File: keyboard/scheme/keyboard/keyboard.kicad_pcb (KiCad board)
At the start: 2 copper layers, 53 parts

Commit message: Update keyboard pcd
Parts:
- removed the REF** at (62.9, 64.1)
- removed the REF** at (29.8, 88.9)
- removed the REF** at (79.4, 97.2)
- removed the REF** at (29.8, 64.1)
- removed the REF** at (104.1, 64.1)
- removed the REF** at (95.9, 64.1)
- removed the REF** at (112.4, 80.6)
- removed the REF** at (46.4, 97.2)
- removed the REF** at (71.1, 64.1)
- removed the REF** at (38.1, 64.1)
- removed the REF** at (38.1, 88.9)
- removed the REF** at (38.1, 97.2)
- removed the REF** at (112.4, 72.4)
- removed the REF** at (34.3, 80.6)
- removed the REF** at (46.4, 72.4)
- removed the REF** at (79.4, 64.1)
- removed the REF** at (29.8, 97.2)
- removed the REF** at (46.4, 88.9)
- removed the REF** at (46.4, 64.1)
- removed the REF** at (54.6, 64.1)
- removed the REF** at (87.6, 64.1)
- removed the REF** at (112.4, 64.1)
- removed the REF** at (38.1, 72.4)
- removed the REF** at (29.8, 72.4)
- removed the REF** at (42.5, 80.6)
- removed the REF** at (50.8, 80.6)
- added SW1: SW_DIP_x01, my_lib:btn_8x8, F.Cu at (48.9, 88.6)
- added SW10: SW_DIP_x01, my_lib:btn_8x8, F.Cu at (48.9, 105.1)
- added SW11: SW_DIP_x01, my_lib:btn_8x8, F.Cu at (57.1, 105.1)
- added SW12: SW_DIP_x01, my_lib:btn_8x8, F.Cu at (57.1, 113.3)
- added SW13: SW_DIP_x01, my_lib:btn_8x8, F.Cu at (73.7, 88.6)
- added SW14: SW_DIP_x01, my_lib:btn_8x8, F.Cu at (65.4, 88.6)
- added SW15: SW_DIP_x01, my_lib:btn_8x8, F.Cu at (78.1, 96.8)
- added SW16: SW_DIP_x01, my_lib:btn_8x8, F.Cu at (69.8, 96.8)
- added SW17: SW_DIP_x01, my_lib:btn_8x8, F.Cu at (65.4, 105.1)
- added SW18: SW_DIP_x01, my_lib:btn_8x8, F.Cu at (73.7, 105.1)
- added SW19: SW_DIP_x01, my_lib:btn_8x8, F.Cu at (81.9, 88.6)
- added SW2: SW_DIP_x01, my_lib:btn_8x8, F.Cu at (40.6, 88.6)
- added SW20: SW_DIP_x01, my_lib:btn_8x8, F.Cu at (90.2, 88.6)
- added SW21: SW_DIP_x01, my_lib:btn_8x8, F.Cu at (81.9, 105.1)
- added SW22: SW_DIP_x01, my_lib:btn_8x8, F.Cu at (86.4, 96.8)
- added SW23: SW_DIP_x01, my_lib:btn_8x8, F.Cu at (90.2, 105.1)
- added SW24: SW_DIP_x01, my_lib:btn_8x8, F.Cu at (73.7, 113.3)
- added SW25: SW_DIP_x01, my_lib:btn_8x8, F.Cu at (98.4, 88.6)
- added SW26: SW_DIP_x01, my_lib:btn_8x8, F.Cu at (94.6, 96.8)
- added SW27: SW_DIP_x01, my_lib:btn_8x8, F.Cu at (102.9, 96.8)
- added SW28: SW_DIP_x01, my_lib:btn_8x8, F.Cu at (106.7, 105.1)
- added SW29: SW_DIP_x01, my_lib:btn_8x8, F.Cu at (98.4, 105.1)
- added SW3: SW_DIP_x01, my_lib:btn_8x8, F.Cu at (45.1, 96.8)
- added SW30: SW_DIP_x01, my_lib:btn_8x8, F.Cu at (98.4, 113.3)
- added SW31: SW_DIP_x01, my_lib:btn_8x8, F.Cu at (106.7, 88.6)
- added SW32: SW_DIP_x01, my_lib:btn_8x8, F.Cu at (114.9, 88.6)
- added SW33: SW_DIP_x01, my_lib:btn_8x8, F.Cu at (111.1, 96.8)
- added SW34: SW_DIP_x01, my_lib:btn_8x8, F.Cu at (114.9, 105.1)
- added SW35: SW_DIP_x01, my_lib:btn_8x8, F.Cu at (114.9, 113.3)
- added SW36: SW_DIP_x01, my_lib:btn_8x8, F.Cu at (106.7, 113.3)
- added SW4: SW_DIP_x01, my_lib:btn_8x8, F.Cu at (40.6, 105.1)
- added SW5: SW_DIP_x01, my_lib:btn_8x8, F.Cu at (40.6, 113.3)
- added SW6: SW_DIP_x01, my_lib:btn_8x8, F.Cu at (48.9, 113.3)
- added SW7: SW_DIP_x01, my_lib:btn_8x8, F.Cu at (57.1, 88.6)
- added SW8: SW_DIP_x01, my_lib:btn_8x8, F.Cu at (61.6, 96.8)
- added SW9: SW_DIP_x01, my_lib:btn_8x8, F.Cu at (53.3, 96.8)
- added U1: STM32F030F4Px, Package_SO:TSSOP-20_4.4x6.5mm_P0.65mm, F.Cu at (69.8, 119.7)
- moved REF** 38.8 mm to (71.5, 50.1)
- moved REF** 38.8 mm to (104.5, 50.1)
- moved REF** 38.8 mm to (63.2, 50.1)
- moved REF** 38.8 mm to (79.7, 50.1)
- moved REF** 38.8 mm to (55.0, 50.1)
- moved REF** 38.8 mm to (88.0, 50.1)
- moved REF** 38.8 mm to (96.2, 50.1)
- moved REF** 38.8 mm to (88.0, 58.4)
- moved REF** 38.8 mm to (55.0, 33.6)
- moved REF** 38.8 mm to (104.5, 58.4)
- moved REF** 38.8 mm to (63.2, 58.4)
- moved REF** 38.8 mm to (104.5, 33.6)
- moved REF** 38.8 mm to (79.7, 33.6)
- moved REF** 38.8 mm to (63.2, 33.6)
- moved REF** 38.8 mm to (52.1, 56.5)
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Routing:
- net row_2: track 0.00 -> 227.6 mm, vias 0 -> 1
- net row_3: track 0.00 -> 174.9 mm, vias 0 -> 1
- net row_1: track 0.00 -> 158.2 mm, vias 0 -> 1
- net row_4: track 0.00 -> 141.3 mm, vias 0 -> 1
- net row_5: track 0.00 -> 134.0 mm, vias 0 -> 1
- net row_6: track 0.00 -> 94.6 mm, vias 0 -> 1
- net column_6: track 0.00 -> 84.9 mm
- net column_1: track 0.00 -> 83.1 mm
- net column_5: track 0.00 -> 76.0 mm
- net column_2: track 0.00 -> 61.7 mm
- net column_3: track 0.00 -> 61.6 mm
- net column_4: track 0.00 -> 61.2 mm
- net sw_dio: track 0.00 -> 16.2 mm, vias 0 -> 1
- net sw_clk: track 0.00 -> 11.2 mm, vias 0 -> 1

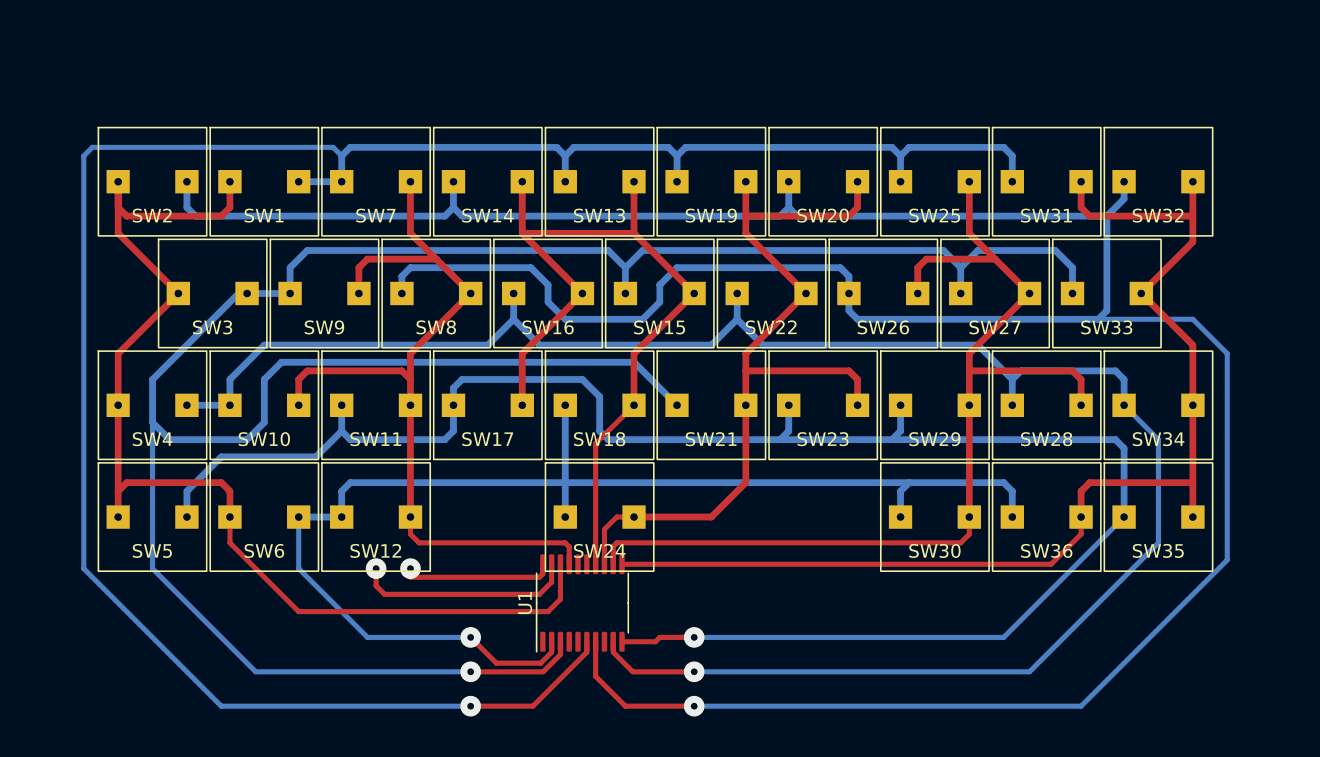
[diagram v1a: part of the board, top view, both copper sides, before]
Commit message: Add power supply to keyboard scheme
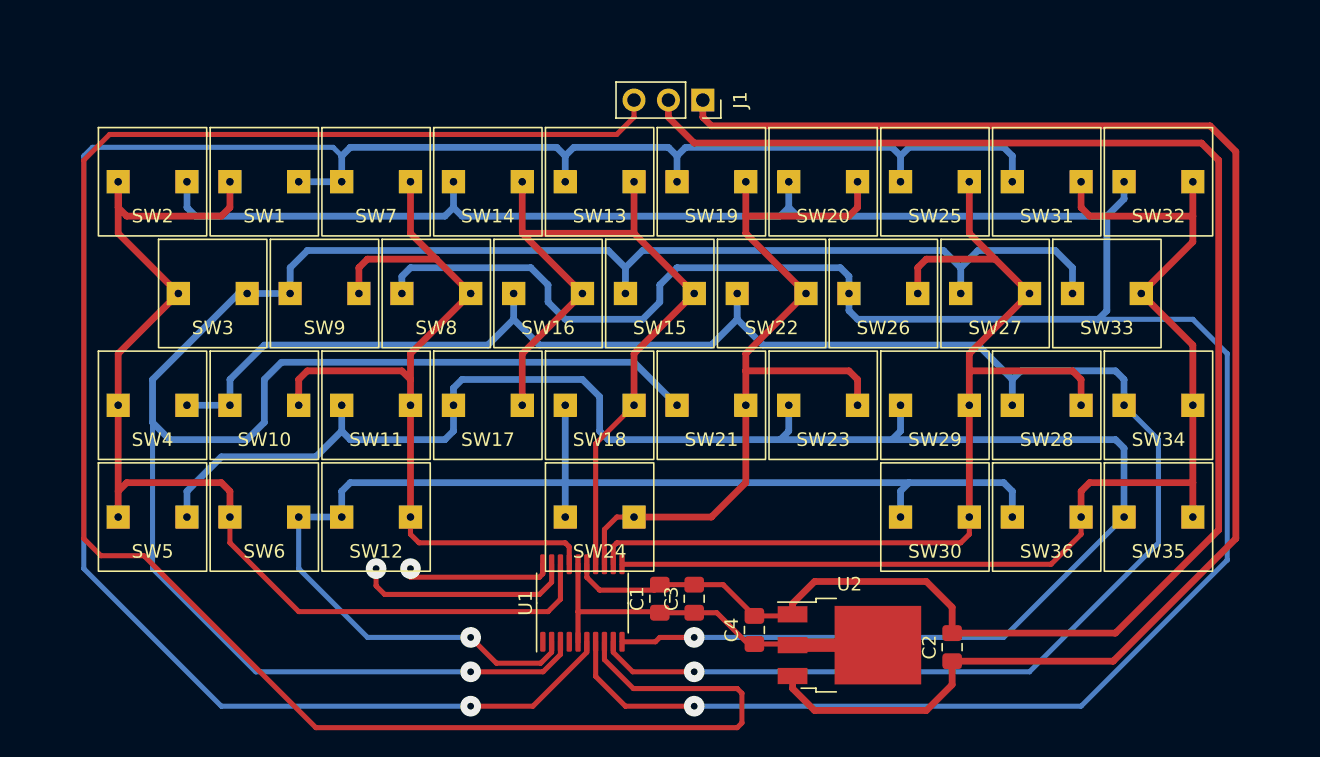
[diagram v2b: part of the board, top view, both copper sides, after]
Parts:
- added C1: 100nF, Capacitor_SMD:C_0805_2012Metric_Pad1.18x1.45mm_HandSolder, F.Cu at (75.6, 119.4)
- added C2: 10mF, Capacitor_SMD:C_0805_2012Metric_Pad1.18x1.45mm_HandSolder, F.Cu at (97.2, 123.0)
- added C3: 4.7mF, Capacitor_SMD:C_0805_2012Metric_Pad1.18x1.45mm_HandSolder, F.Cu at (78.1, 119.4)
- added C4: 22mF, Capacitor_SMD:C_0805_2012Metric_Pad1.18x1.45mm_HandSolder, F.Cu at (82.5, 121.7)
- added J1: Conn_01x03, Connector_PinSocket_2.54mm:PinSocket_1x03_P2.54mm_Vertical, F.Cu at (78.7, 82.5)
- added U2: AMS1117CD-3.3, Package_TO_SOT_SMD:TO-252-3_TabPin2, F.Cu at (89.6, 122.8)
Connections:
- U1 pad 15: unconnected-(U1-Pad15) -> GND
- U1 pad 16: unconnected-(U1-Pad16) -> 3.3v
- U1 pad 5: unconnected-(U1-Pad5) -> 3.3v
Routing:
- net uart_tx: track 0.00 -> 140.4 mm
- net GND: track 0.00 -> 127.0 mm
- net 5v: track 0.00 -> 110.9 mm
- net 3.3v: track 0.00 -> 28.9 mm

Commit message: Some fix keyboard scheme
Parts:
- removed REF**: PinHeader_1x07_P2.54mm_Vertical, Connector_PinHeader_2.54mm:PinHeader_1x07_P2.54mm_Vertical
- removed REF** (x24): btn_8x8, my_footprints:btn_8x8
- removed REF**: PinHeader_1x08_P2.54mm_Vertical, Connector_PinHeader_2.54mm:PinHeader_1x08_P2.54mm_Vertical
- removed REF**: R_1206_3216Metric_Pad1.30x1.75mm_HandSolder, Resistor_SMD:R_1206_3216Metric_Pad1.30x1.75mm_HandSolder
- moved J1 2.13 mm to (77.8, 84.5)
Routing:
- net (no net): track 1683.9 -> 0.00 mm
- net uart_tx: track 140.4 -> 137.9 mm
- net GND: track 127.0 -> 127.8 mm
- net 5v: track 110.9 -> 110.3 mm

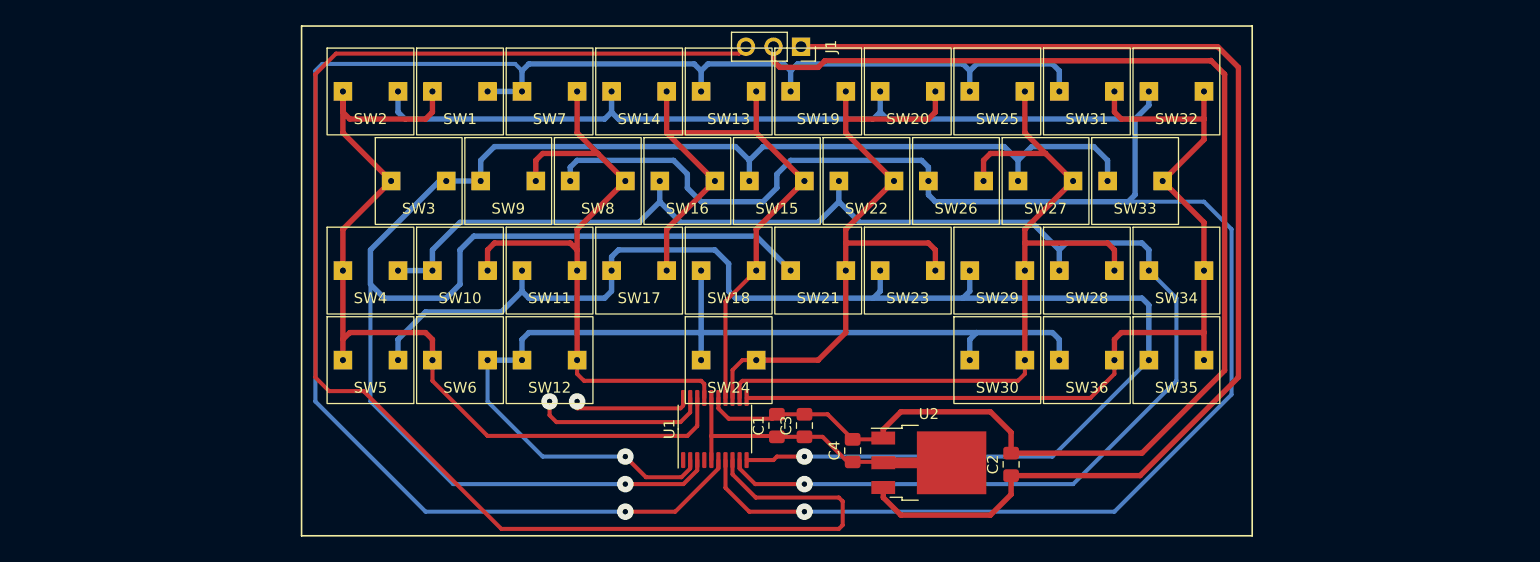
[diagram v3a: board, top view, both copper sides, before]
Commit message: Add copyright to keyboard scheme
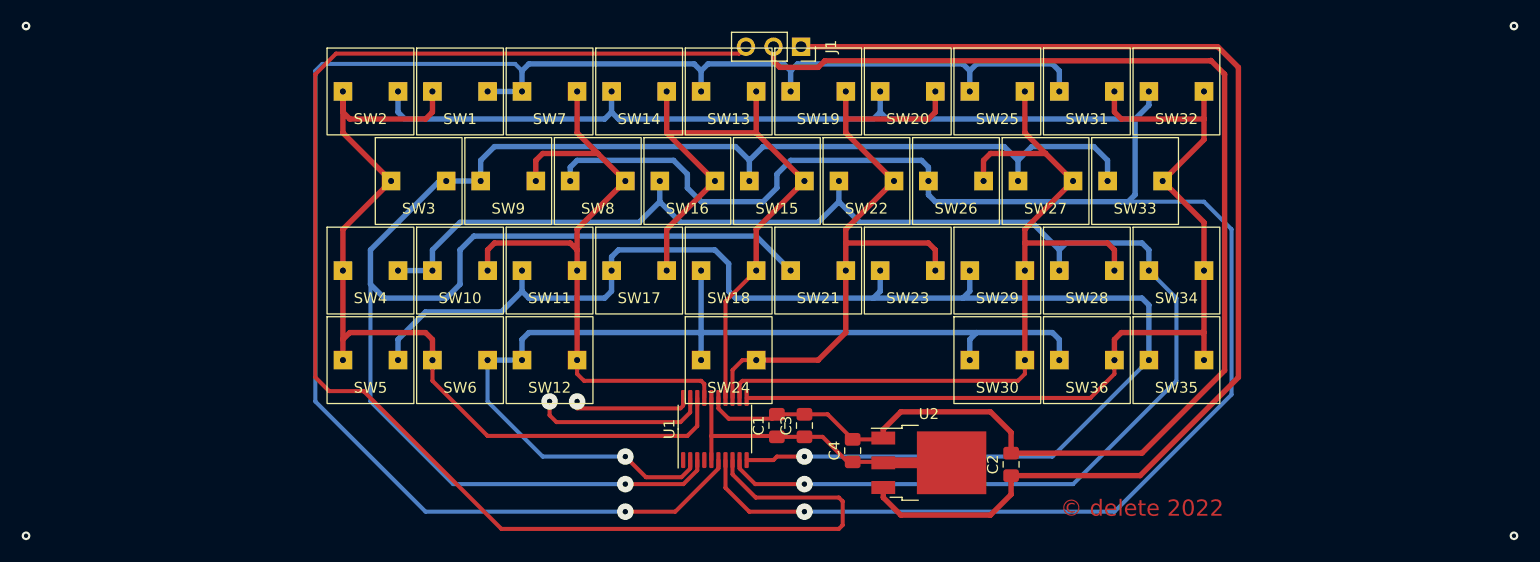
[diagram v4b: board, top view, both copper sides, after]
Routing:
- net (no net): vias 0 -> 4
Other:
- board text added: "© delete 2022"
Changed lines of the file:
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@@
     )
   )
-  (gr_rect (start 119.38 129.54) (end 31.75 82.55) (layer "F.SilkS") (width 0.15) (fill none))
+  (gr_rect (start 119.38 129.54) (end 31.75 82.55) (layer "F.Mask") (width 0.15) (fill none))
+  (gr_text "© delete 2022" (at 109.22 127) (layer "F.Cu")
+    (effects (font (size 1.5 1.5) (thickness 0.3)))
+  )
+  (via (at 143.51 82.55) (size 0.8) (drill 0.4) (layers "F.Cu" "B.Cu") (free) (net 0))
+  (via (at 6.35 129.54) (size 0.8) (drill 0.4) (layers "F.Cu" "B.Cu") (free) (net 0))
+  (via (at 6.35 82.55) (size 0.8) (drill 0.4) (layers "F.Cu" "B.Cu") (free) (net 0))
+  (via (at 143.51 129.54) (size 0.8) (drill 0.4) (layers "F.Cu" "B.Cu") (free) (net 0))
   (segment (start 82.085 122.725) (end 79.7775 120.4175) (width 0.375) (layer "F.Cu") (net 3))
   (segment (start 75.565 120.4175) (end 78.105 120.4175) (width 0.375) (layer "F.Cu") (net 3))

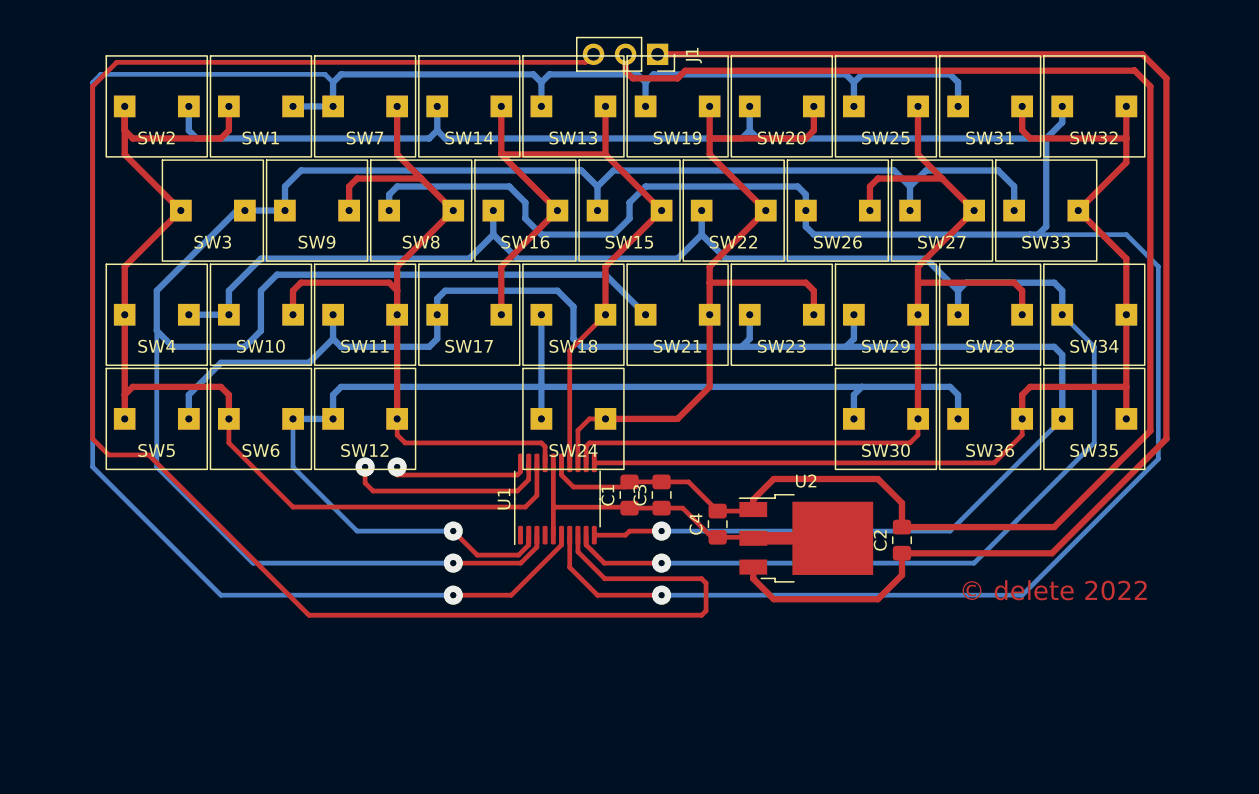
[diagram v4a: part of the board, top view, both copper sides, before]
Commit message: 75% one layer
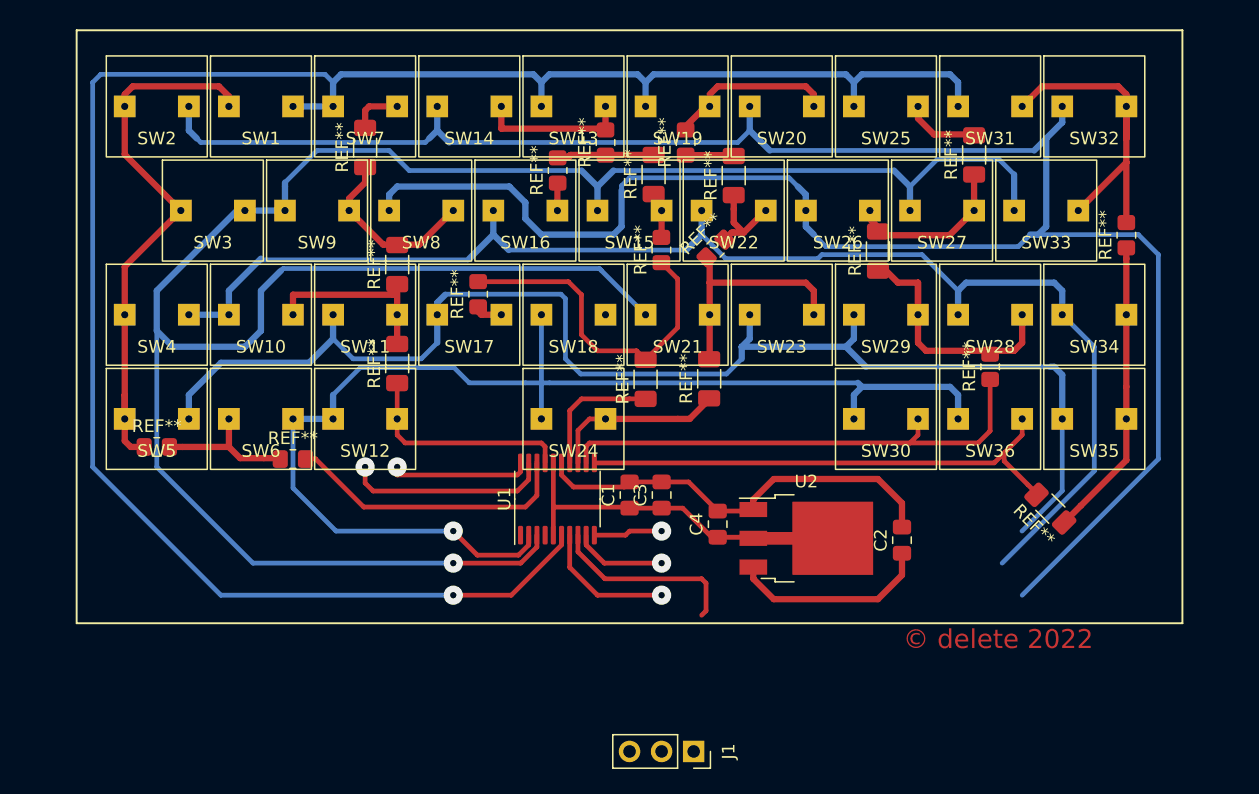
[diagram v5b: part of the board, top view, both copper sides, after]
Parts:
- added REF**: R_0805_2012Metric_Pad1.20x1.40mm_HandSolder, Resistor_SMD:R_0805_2012Metric_Pad1.20x1.40mm_HandSolder, F.Cu at (48.9, 116.5)
- added REF**: R_0805_2012Metric_Pad1.20x1.40mm_HandSolder, Resistor_SMD:R_0805_2012Metric_Pad1.20x1.40mm_HandSolder, F.Cu at (78.1, 100.0)
- added REF**: R_1206_3216Metric_Pad1.30x1.75mm_HandSolder, Resistor_SMD:R_1206_3216Metric_Pad1.30x1.75mm_HandSolder, F.Cu at (76.8, 110.2)
- added REF**: R_0805_2012Metric_Pad1.20x1.40mm_HandSolder, Resistor_SMD:R_0805_2012Metric_Pad1.20x1.40mm_HandSolder, F.Cu at (38.1, 115.6)
- added REF**: R_0805_2012Metric_Pad1.20x1.40mm_HandSolder, Resistor_SMD:R_0805_2012Metric_Pad1.20x1.40mm_HandSolder, F.Cu at (69.9, 93.7)
- added REF**: R_1206_3216Metric_Pad1.30x1.75mm_HandSolder, Resistor_SMD:R_1206_3216Metric_Pad1.30x1.75mm_HandSolder, F.Cu at (95.2, 100.0)
- added REF**: R_1206_3216Metric_Pad1.30x1.75mm_HandSolder, Resistor_SMD:R_1206_3216Metric_Pad1.30x1.75mm_HandSolder, F.Cu at (83.8, 94.1)
- added REF**: R_1206_3216Metric_Pad1.30x1.75mm_HandSolder, Resistor_SMD:R_1206_3216Metric_Pad1.30x1.75mm_HandSolder, F.Cu at (102.9, 92.4)
- added REF**: R_0805_2012Metric_Pad1.20x1.40mm_HandSolder, Resistor_SMD:R_0805_2012Metric_Pad1.20x1.40mm_HandSolder, F.Cu at (114.9, 98.8)
- added REF**: R_0805_2012Metric_Pad1.20x1.40mm_HandSolder, Resistor_SMD:R_0805_2012Metric_Pad1.20x1.40mm_HandSolder, F.Cu at (104.1, 109.2)
- added REF**: R_0805_2012Metric_Pad1.20x1.40mm_HandSolder, Resistor_SMD:R_0805_2012Metric_Pad1.20x1.40mm_HandSolder, F.Cu at (73.7, 91.4)
- added REF**: R_1206_3216Metric_Pad1.30x1.75mm_HandSolder, Resistor_SMD:R_1206_3216Metric_Pad1.30x1.75mm_HandSolder, F.Cu at (57.2, 101.1)
- added REF**: R_0805_2012Metric_Pad1.20x1.40mm_HandSolder, Resistor_SMD:R_0805_2012Metric_Pad1.20x1.40mm_HandSolder, F.Cu at (82.4, 99.8)
- added REF**: R_1206_3216Metric_Pad1.30x1.75mm_HandSolder, Resistor_SMD:R_1206_3216Metric_Pad1.30x1.75mm_HandSolder, F.Cu at (54.6, 91.8)
- added REF**: R_1206_3216Metric_Pad1.30x1.75mm_HandSolder, Resistor_SMD:R_1206_3216Metric_Pad1.30x1.75mm_HandSolder, F.Cu at (57.1, 109.0)
- added REF**: R_1206_3216Metric_Pad1.30x1.75mm_HandSolder, Resistor_SMD:R_1206_3216Metric_Pad1.30x1.75mm_HandSolder, F.Cu at (81.9, 110.2)
- added REF**: R_0805_2012Metric_Pad1.20x1.40mm_HandSolder, Resistor_SMD:R_0805_2012Metric_Pad1.20x1.40mm_HandSolder, F.Cu at (63.6, 103.5)
- added REF**: R_0805_2012Metric_Pad1.20x1.40mm_HandSolder, Resistor_SMD:R_0805_2012Metric_Pad1.20x1.40mm_HandSolder, F.Cu at (80.0, 91.4)
- added REF**: R_1206_3216Metric_Pad1.30x1.75mm_HandSolder, Resistor_SMD:R_1206_3216Metric_Pad1.30x1.75mm_HandSolder, F.Cu at (77.5, 94.0)
- added REF**: R_1206_3216Metric_Pad1.30x1.75mm_HandSolder, Resistor_SMD:R_1206_3216Metric_Pad1.30x1.75mm_HandSolder, F.Cu at (108.9, 120.5)
- moved J1 55.3 mm to (80.6, 139.7)
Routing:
- net uart_tx: track 137.9 -> 15.2 mm
- net 5v: track 110.3 -> 15.9 mm
- net GND: track 127.8 -> 33.7 mm
- net (no net): track 0.00 -> 38.7 mm
- net column_3: track 61.6 -> 29.2 mm
- net row_4: track 141.3 -> 115.4 mm
- net row_2: track 227.6 -> 203.5 mm
- net row_5: track 134.0 -> 112.1 mm
- net column_2: track 61.7 -> 50.1 mm
- net column_4: track 61.2 -> 52.0 mm
- net column_6: track 84.9 -> 91.2 mm
- net column_5: track 76.0 -> 80.1 mm
- net row_3: track 174.9 -> 178.1 mm
- net column_1: track 83.1 -> 79.9 mm
- net row_6: track 94.6 -> 96.8 mm
